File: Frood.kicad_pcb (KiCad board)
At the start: 2 copper layers, 17.8 x 33.5 mm, 41 parts, among them J1 Left, J2 Right, J3 Bottom, SW1 RESET, SW2 BOOT, U1 RP2040, U2 W25Q32JWUUIQ, U3 TLV73333PDBVR, Y1 X322512MSB4SI

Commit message: Rename to Frood; use a 500 mA regulator; update README
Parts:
- U3: value TLV73333PDBVR -> SPX3819M5-L-3-3/TR
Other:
- board text added: "The Frood"
- board text added: "The Frood rev3 42Keebs.eu 2022"
- board text removed: "PiMicro2040 rev3 42Keebs.eu 2022"

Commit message: Fix the USB-C socket value; Use an in-stock 27R resistor
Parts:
- USB1: value HRO-TYPE-C-31-M-13 -> HRO-TYPE-C-31-M-14
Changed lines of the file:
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@@
       (effects (font (size 0.5 0.5) (thickness 0.1)))
     )
-    (fp_text value "HRO-TYPE-C-31-M-13" (at 0.025 -7.9) (layer "F.Fab") hide
+    (fp_text value "HRO-TYPE-C-31-M-14" (at 0.025 -7.9) (layer "F.Fab") hide
       (effects (font (size 0.5 0.5) (thickness 0.1)))
     )

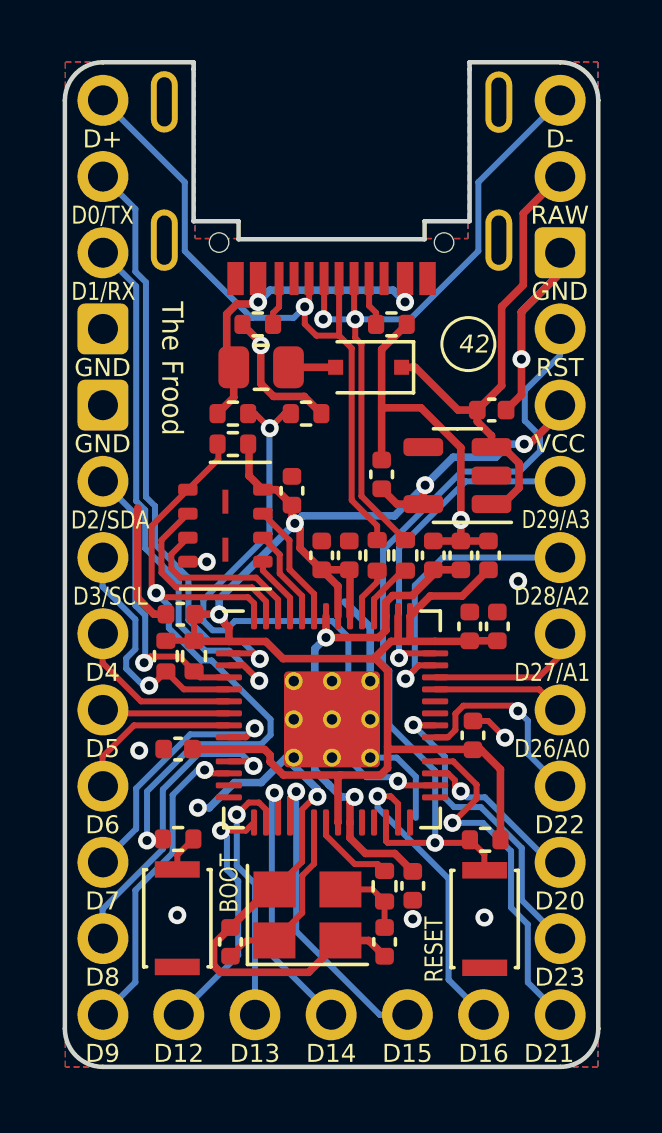
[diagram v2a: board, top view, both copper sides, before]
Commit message: Drop the forced I2C pull-up resistors; Add flash 3D model
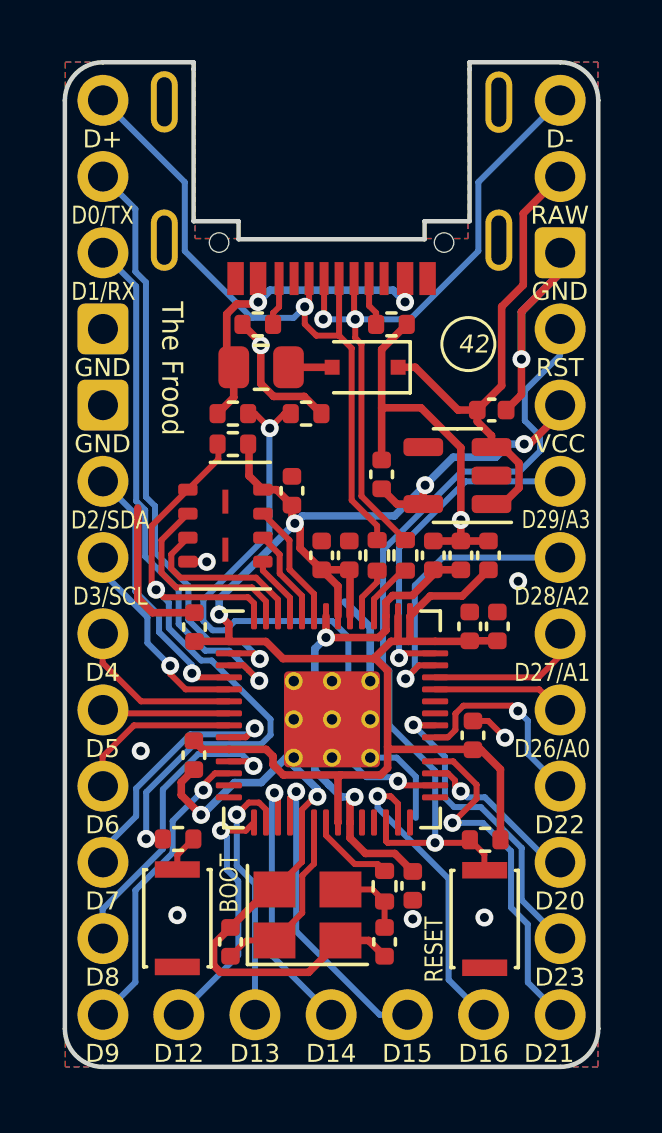
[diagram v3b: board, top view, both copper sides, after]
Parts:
- removed R10, R9: 5.1k, Resistor_SMD:R_0402_1005Metric
- moved C13 0.64 mm to (121.7, 73.8), turned to 90 degrees
- moved C15 0.56 mm to (121.7, 78.1), turned to -90 degrees
- moved D1 0.11 mm to (127.4, 65.2)
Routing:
- net GND: track 59.2 -> 62.0 mm
- net +3V3: track 64.9 -> 62.3 mm
- net /D3/SCL: track 8.38 -> 6.98 mm
- net /D2/SDA: track 9.85 -> 8.92 mm
